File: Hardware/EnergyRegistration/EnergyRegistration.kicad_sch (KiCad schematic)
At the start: 17 parts

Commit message: Vorking commit
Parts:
- removed A?: Arduino_Ethernet_REV3, Module:Arduino_Ethernet_REV3, symbol ArduinoBoards:Arduino_Ethernet_REV3
- removed J?: Screw_Terminal_01x08, symbol ArduinoEthernet-rescue:Screw_Terminal_01x08-Connector
- added A?: Arduino_Ethernet_REV3, Module:Arduino_Ethernet_REV3, symbol Local_MCU_Module_Library:Arduino_Ethernet_REV3
- added J?: Barrel_Jack_MountingPin, symbol Connector:Barrel_Jack_MountingPin
- added J? (x2): Screw_Terminal_01x04, symbol Connector:Screw_Terminal_01x04
- added J?: Screw_Terminal_01x02, symbol Connector:Screw_Terminal_01x02
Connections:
- net VCC is gone; now on an unnamed net: R?.1
- net GND: now also A?.29 (GND), A?.33 (GND), A?.34 (GND), A?.6 (GND), A?.7 (GND), J?.2, J?.4 (Pin_4)
- net at Q?.1 (C): now also A?.17 (D2/INT0)
- net at Q?.3 (E): now also A?.5 (+5V)
- net at D?.1 (K): now also A?.10 (A1), J?.3 (Pin_3)
- net at D?.1 (K): now also A?.9 (A0), J?.2 (Pin_2)
- net at D?.1 (K): now also A?.23 (D8), J?.1 (Pin_1)
- net at D?.1 (K): now also A?.22 (D7), J?.4 (Pin_4)
- net at D?.1 (K): now also D?.1 (K), D?.1 (K), A?.18 (D3/INT1), A?.20 (D5), A?.21 (D6), J?.1 (Pin_1), J?.2 (Pin_2), J?.3 (Pin_3)
- net at R?.1: now also A?.24 (D9/CS)
- new net: A?.8 (VIN), J?.1

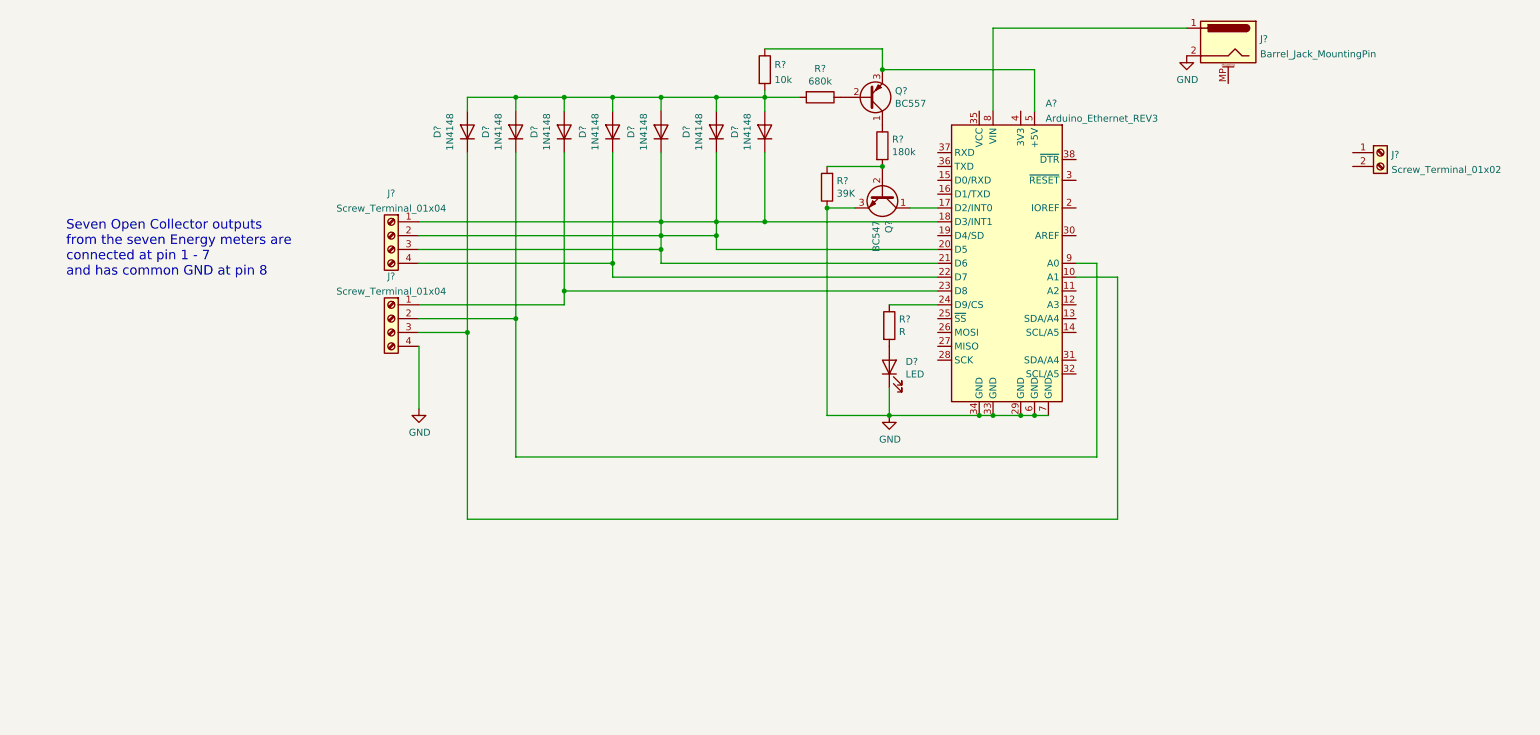
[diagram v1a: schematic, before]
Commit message: PCB Components added
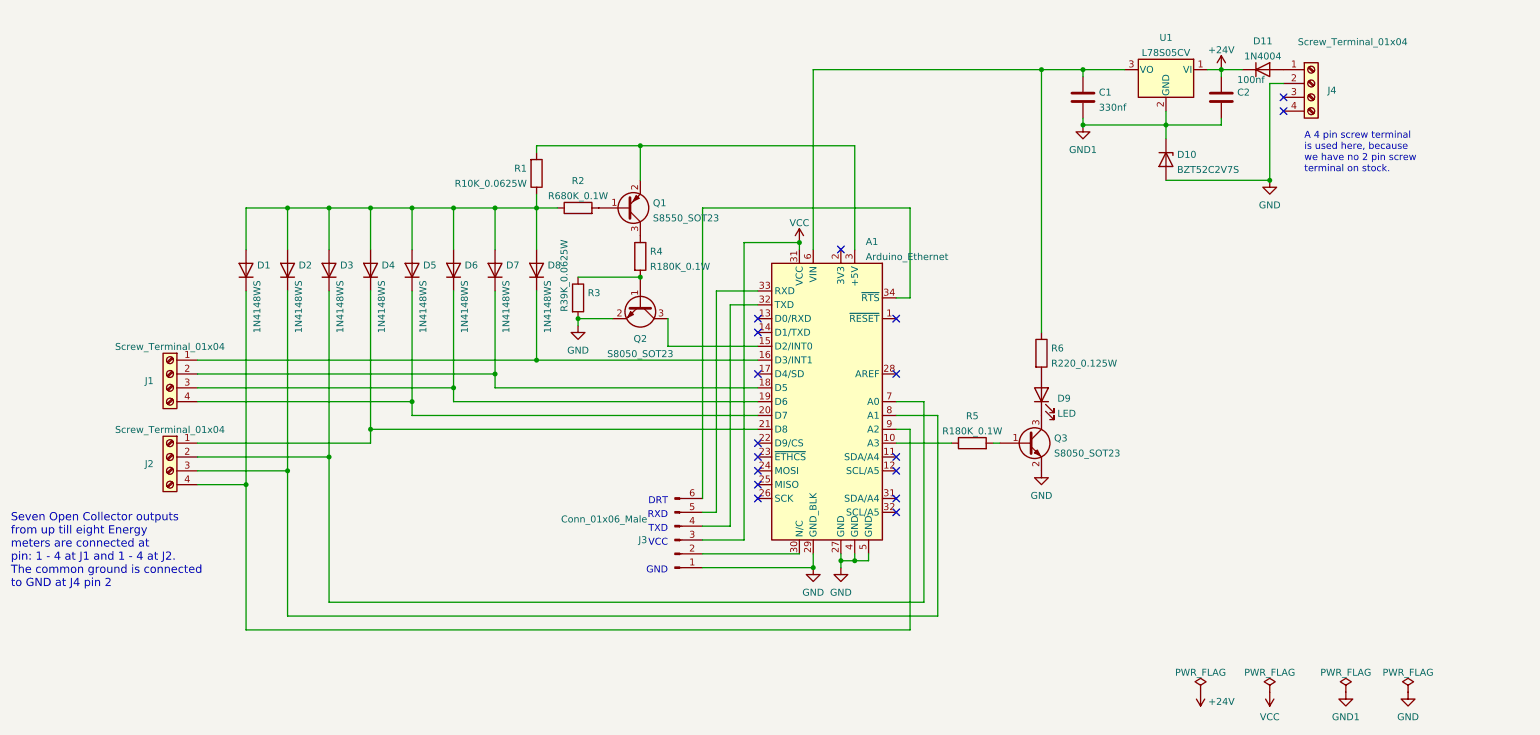
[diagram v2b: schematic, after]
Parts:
- removed A?: Arduino_Ethernet_REV3, Module:Arduino_Ethernet_REV3, symbol Local_MCU_Module_Library:Arduino_Ethernet_REV3
- removed D? (x7): 1N4148, Diode_THT:D_DO-35_SOD27_P7.62mm_Horizontal, symbol ArduinoEthernet-rescue:1N4148-Diode
- removed D?: LED, symbol ArduinoEthernet-rescue:LED-Device
- removed J?: Barrel_Jack_MountingPin, symbol Connector:Barrel_Jack_MountingPin
- removed J?: Screw_Terminal_01x02, symbol Connector:Screw_Terminal_01x02
- removed Q?: BC547, Package_TO_SOT_THT:TO-92_Inline, symbol ArduinoEthernet-rescue:BC547-Transistor_BJT
- removed Q?: BC557, Package_TO_SOT_THT:TO-92_Inline, symbol ArduinoEthernet-rescue:BC557-Transistor_BJT
- removed R?: 39K, symbol ArduinoEthernet-rescue:R-Device
- removed R?: 180k, symbol ArduinoEthernet-rescue:R-Device
- removed R?: 680k, symbol ArduinoEthernet-rescue:R-Device
- removed R?: R, symbol ArduinoEthernet-rescue:R-Device
- removed R?: 10k, symbol Device:R
- added A1: Arduino_Ethernet, Local_MCU_Module_Library:Arduino_Ethernet_WithMountingHoles, symbol Local_MCU_Module_Library:Arduino_Ethernet
- added C1: 330nf, Capacitor_SMD:C_0805_2012Metric, symbol Device:C
- added C2: 100nf, Capacitor_SMD:C_0805_2012Metric, symbol Device:C
- added D1, D2, D3, D4, D5, D6, D7, D8: 1N4148WS, Diode_SMD:D_SOD-323F, symbol Diode:1N4148
- added D10: BZT52C2V7S, Diode_SMD:D_SOD-123, symbol Diode:BZT52Bxx
- added D11: 1N4004, Diode_THT:D_DO-41_SOD81_P10.16mm_Horizontal, symbol Diode:1N4004
- added D9: LED, LED_THT:LED_D3.0mm, symbol Device:LED
- added J3: Conn_01x06_Male, Local_Connectors:PinHeader_1x06_P2.50mm_Vertical, symbol Connector:Conn_01x06_Male
- added J4: Screw_Terminal_01x04, Local_Connectors:TerminalBlock_PT-1,5-4-5.0-H_1x04_P5.00mm_Horizontal-(Frontside-Mount), symbol Connector:Screw_Terminal_01x04
- added Q1: S8550_SOT23, Package_TO_SOT_SMD:SOT-23, symbol Local_Transistor_BJT_Library:S8550_SOT23
- added Q2, Q3: S8050_SOT23, Package_TO_SOT_SMD:SOT-23, symbol Local_Transistor_BJT_Library:S8050_SOT23
- added R1: R10K_0.0625W, Resistor_SMD:R_0603_1608Metric, symbol Local_Device_Library:R10K_0.0625W
- added R2: R680K_0.1W, Resistor_SMD:R_0603_1608Metric, symbol Local_Device_Library:R680K_0.1W
- added R3: R39K_0.0625W, Resistor_SMD:R_0402_1005Metric, symbol Local_Device_Library:R39K_0.0625W
- added R4, R5: R180K_0.1W, Resistor_SMD:R_0603_1608Metric, symbol Local_Device_Library:R180K_0.1W
- added R6: R220_0.125W, Resistor_SMD:R_0805_2012Metric, symbol Local_Device_Library:R220_0.125W
- added U1: L78S05CV, Package_TO_SOT_THT:TO-220-3_Vertical, symbol Local_Miscellaneous_Library:L78S75CV_TO220AB
- J1, J2: renamed from J?; footprint (none) -> Local_Connectors:TerminalBlock_PT-1,5-4-5.0-H_1x04_P5.00mm_Horizontal-(Frontside-Mount); now left out of the parts list
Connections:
- net GND: now also A1.27 (GND), A1.29 (GND_BLK), A1.4 (GND), A1.5 (GND), D10.2 (A), J3.1 (Pin_1), J4.2 (Pin_2), Q2.2 (E), Q3.2 (E), R3.2; no longer J2.4 (Pin_4)
- net at J2.3 (Pin_3): now also A1.8 (A1), D2.1 (K)
- net at J2.2 (Pin_2): now also A1.7 (A0), D3.1 (K)
- net at J2.1 (Pin_1): now also A1.21 (D8), D4.1 (K)
- net at J1.4 (Pin_4): now also A1.20 (D7), D5.1 (K)
- new net: Q1.3 (C), R4.1
- new net: Q2.1 (B), R3.1, R4.2
- new net: Q1.1 (B), R2.2
- new net: A1.3 (+5V), Q1.2 (E), R1.2
- new net: D1.2 (A), D2.2 (A), D3.2 (A), D4.2 (A), D5.2 (A), D6.2 (A), D7.2 (A), D8.2 (A), R1.1, R2.1
- new net: A1.9 (A2), D1.1 (K), J2.4 (Pin_4)
- new net: A1.6 (VIN), C1.1, R6.1, U1.3 (VO)
- new net: A1.16 (D3/INT1), D8.1 (K), J1.1 (Pin_1)
- new net: A1.18 (D5), D7.1 (K), J1.2 (Pin_2)
- new net: A1.19 (D6), D6.1 (K), J1.3 (Pin_3)
- new net: A1.10 (A3), R5.1
- new net: Q3.1 (B), R5.2
- new net: A1.15 (D2/INT0), Q2.3 (C)
- new net: D9.1 (K), Q3.3 (C)
- new net: D9.2 (A), R6.2
- new net: A1.30 (N/C), J3.2 (Pin_2)
- new net: A1.32 (TXD), J3.4 (Pin_4)
- new net: A1.33 (RXD), J3.5 (Pin_5)
- new net: A1.34 (~{RTS}), J3.6 (Pin_6)
- new net: D11.2 (A), J4.1 (Pin_1)
- new net +24V: C2.1, D11.1 (K), U1.1 (VI)
- new net GND1: C1.2, C2.2, D10.1 (K), U1.2 (GND)
- new net VCC: A1.31 (VCC), J3.3 (Pin_3)
- no-connect marks 0 -> 17
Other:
- note added: "A 4 pin screw terminal is used here, because we have no 2 pin screw terminal on stock."
- note added: "DRT"
- note added: "GND"
- note added: "RXD"
- note added: "Seven Open Collector outputs from up till eight Energy meters are connected at pin: 1 - 4 at J1 and 1 - 4 at J2. The common ground is connected to GND at J4 pin 2"
- note added: "TXD"
- note added: "VCC"
- note removed: "Seven Open Collector outputs from the seven Energy meters are connected at pin 1 - 7 and has common GND at pin 8"
- moved on the sheet: J1, J2

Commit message: Components changed to SMD
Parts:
- A1, J1, J2, J4: Excluded from BOM (none) -> YES
- C1: Excluded from BOM (none) -> NO; JLCBCB Part (none) -> https://jlcpcb.com/parts/componentSearch?isFirstLevel=true&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; JLCPCB Basic or Extended (none) -> Basic Part; Manufacturer PN 0805B334K500NTCopy -> 0805B334K500NT
- C2: Excluded from BOM (none) -> NO; JLCBCB Part (none) -> https://jlcpcb.com/parts/componentSearch?isFirstLevel=true&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; JLCPCB Basic or Extended (none) -> Basic Part
- D1, D2, D3, D4, D5, D6, D7, D8, R1, R2, R3, R4, R5, R6: Excluded from BOM (none) -> NO; JLCBCB Part (none) -> https://jlcpcb.com/parts/componentSearch?isSearch=true&sear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; JLCPCB Basic or Extended (none) -> Basic Part
- D10: Excluded from BOM (none) -> NO; JLCBCB Part (none) -> https://jlcpcb.com/parts/componentSearch?isSearch=true&sear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; JLCPCB Basic or Extended (none) -> Extended Part
- D11: footprint Diode_THT:D_DO-41_SOD81_P10.16mm_Horizontal -> Diode_THT:D_DO-41_SOD81_P12.70mm_Horizontal; Category (none) -> Discrete Semiconductor Products; Digi-Key Order no.: (none) -> 641-1999-ND; Excluded from BOM (none) -> YES; Famely (none) -> Diodes - Single; LibPart (none) -> ??; Manufacturer (none) -> Comchip Technology; Manufacturer PN (none) -> 1N4004B-G
- D9: Excluded from BOM (none) -> YES; JLCBCB Part (none) -> https://jlcpcb.com/parts/componentSearch?isSearch=true&sear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; JLCPCB Basic or Extended (none) -> Extended Part; now left out of the parts list
- J3: footprint Local_Connectors:PinHeader_1x06_P2.50mm_Vertical -> Local_Connectors:PinHeader_1x06_P_0,1in_Vertical; Excluded from BOM (none) -> YES
- Q1, Q2, Q3: Excluded from BOM (none) -> NO; JLCBCB Part (none) -> https://jlcpcb.com/parts/componentSearch?isSecondLevel=true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; JLCPCB Basic or Extended (none) -> Basic Part
- U1: Excluded from BOM (none) -> YES; now left out of the parts list
